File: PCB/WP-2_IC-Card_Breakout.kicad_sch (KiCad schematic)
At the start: 2 parts, among them J1 Conn_01x38_Female, J2 Conn_02x19_Odd_Even

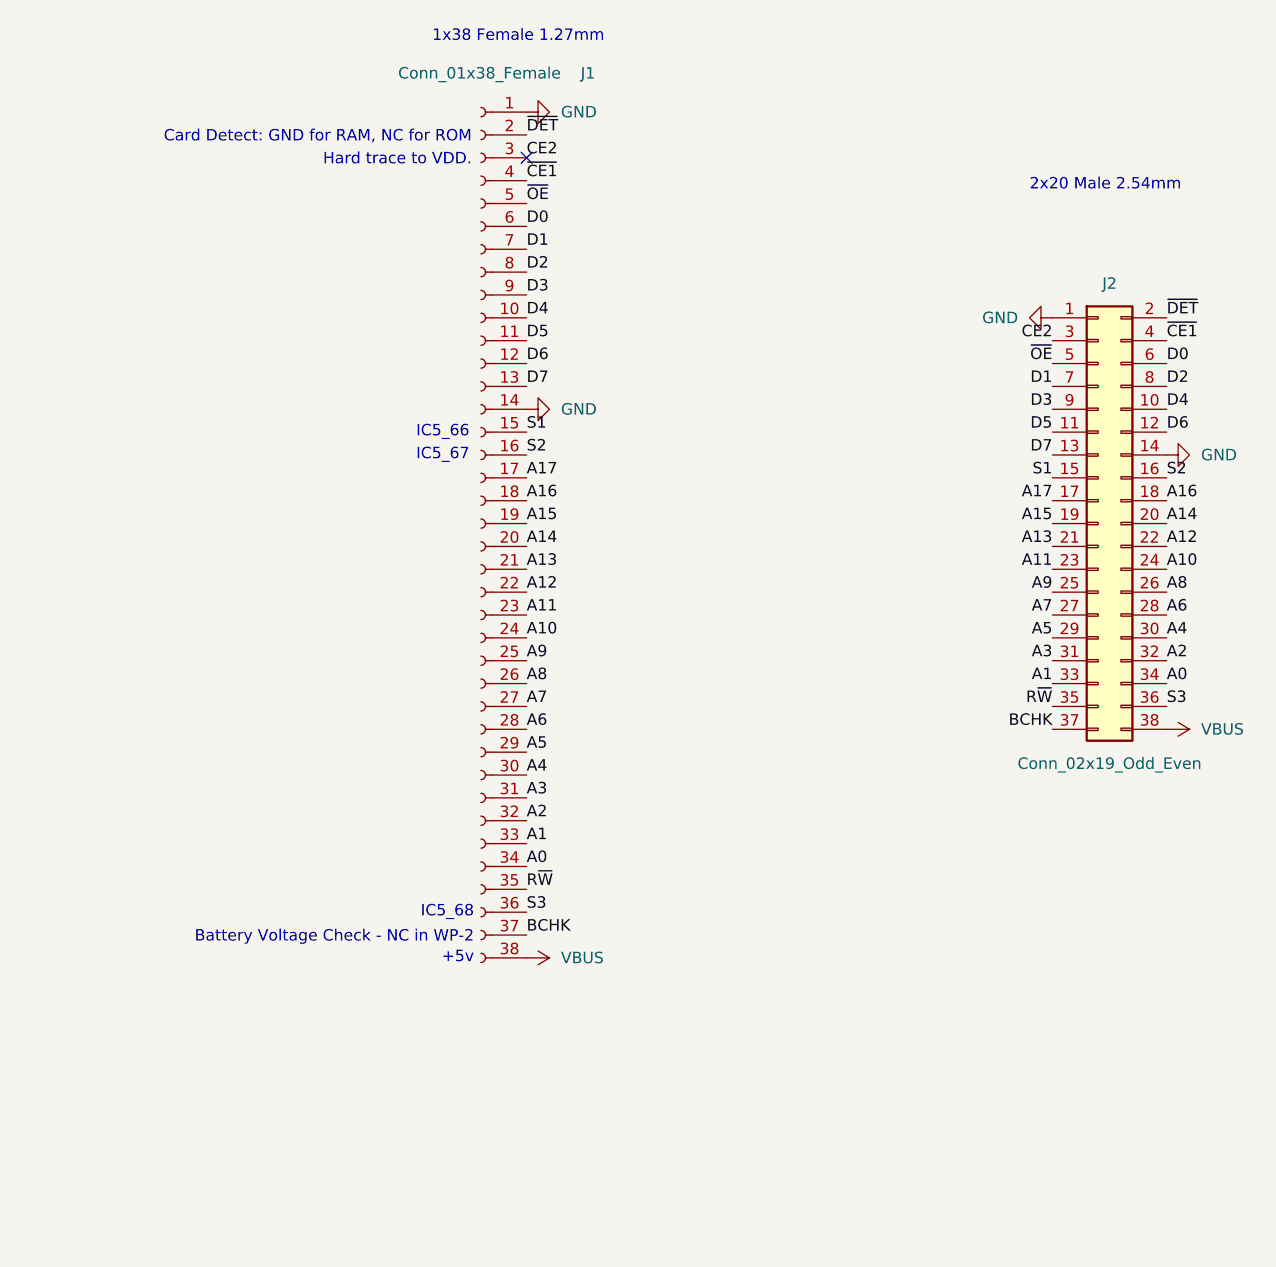
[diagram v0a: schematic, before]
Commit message: MRAM level shifters, delete FRAM, local datasheets in local symbols
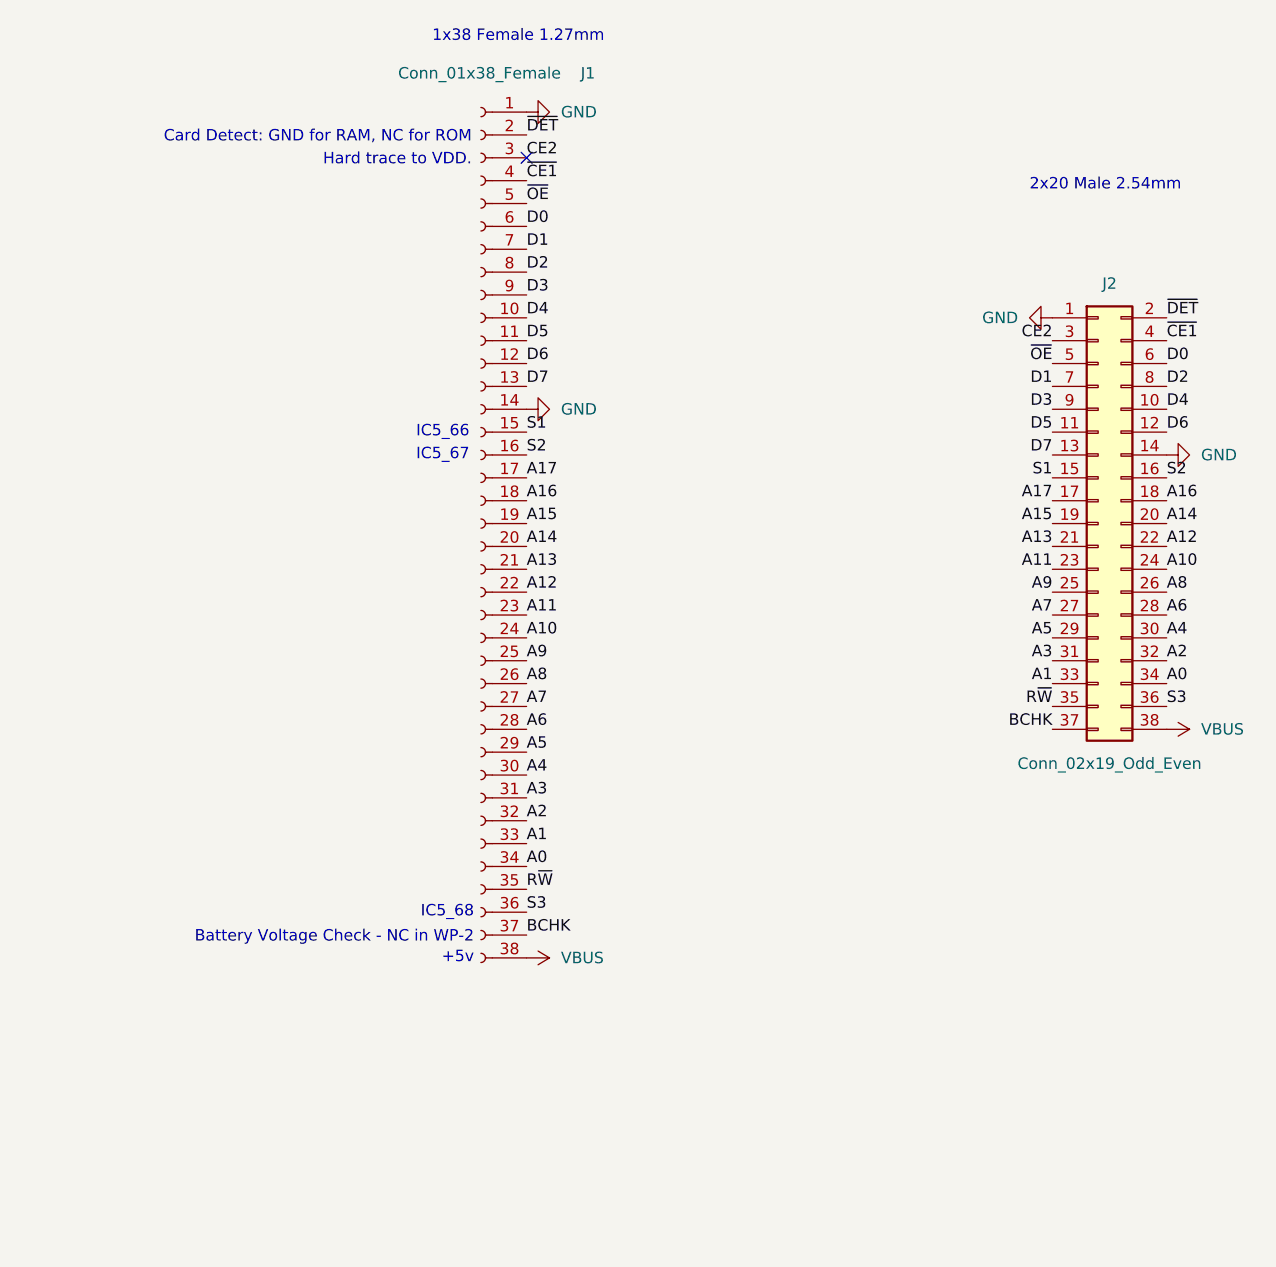
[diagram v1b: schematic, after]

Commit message: local symbol & footprint library organization, add shielded mram version
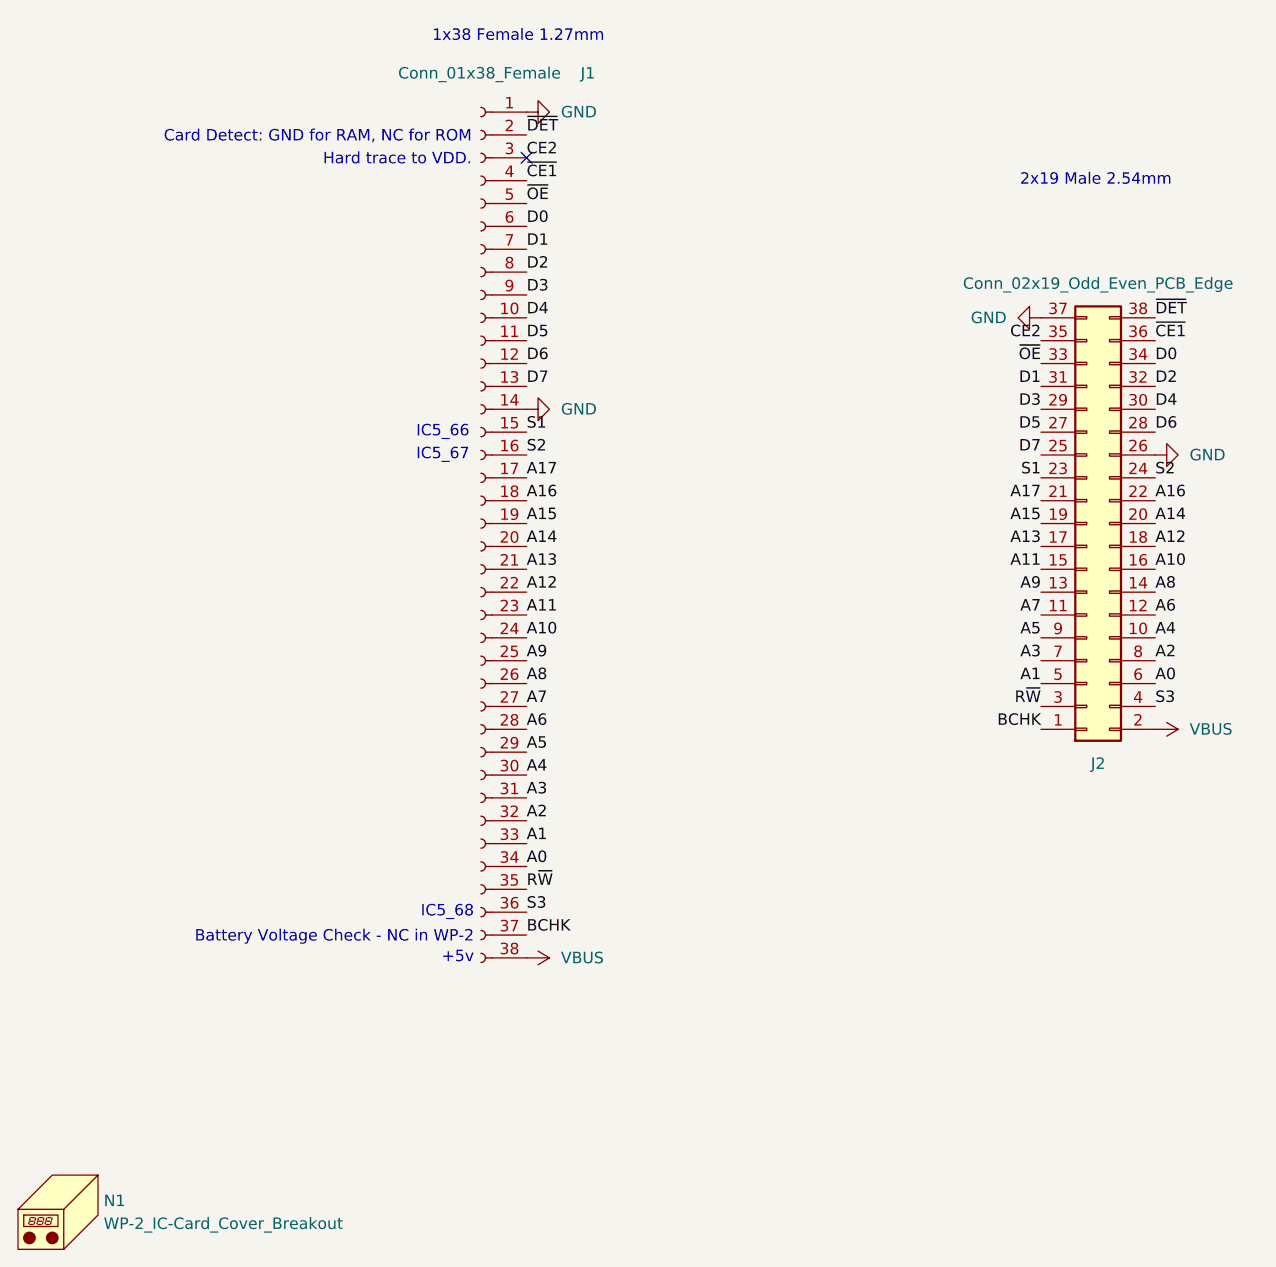
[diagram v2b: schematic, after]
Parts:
- added N1: WP-2_IC-Card_Cover_Breakout, 000_LOCAL:WP-2_IC_Card_Cover_Breakout, symbol 000_LOCAL:Housing
- J1: footprint 0_LOCAL:SMS-138-01-x-x_edge -> 000_LOCAL:SMS-138-01-x-x_pcb_edge; symbol 0_LOCAL:Conn_01x38_Female -> 000_LOCAL:Conn_01x38_Female
- J2: value Conn_02x19_Odd_Even -> Conn_02x19_Odd_Even_PCB_Edge; footprint 0_LOCAL:PinHeader_2x19_P2.54mm -> 000_LOCAL:Pin-Header_2x19_P2.54mm_PCB_Edge; symbol 0_LOCAL:Conn_02x19_Odd_Even -> 000_LOCAL:Conn_02x19_Odd_Even
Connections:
- net A0: now also J2.6 (Pin_6); no longer J2.34 (Pin_34)
- net A1: now also J2.5 (Pin_5); no longer J2.33 (Pin_33)
- net A10: now also J2.16 (Pin_16); no longer J2.24 (Pin_24)
- net A11: now also J2.15 (Pin_15); no longer J2.23 (Pin_23)
- net A12: now also J2.18 (Pin_18); no longer J2.22 (Pin_22)
- net A13: now also J2.17 (Pin_17); no longer J2.21 (Pin_21)
- net A16: now also J2.22 (Pin_22); no longer J2.18 (Pin_18)
- net A17: now also J2.21 (Pin_21); no longer J2.17 (Pin_17)
- net A2: now also J2.8 (Pin_8); no longer J2.32 (Pin_32)
- net A3: now also J2.7 (Pin_7); no longer J2.31 (Pin_31)
- net A4: now also J2.10 (Pin_10); no longer J2.30 (Pin_30)
- net A5: now also J2.9 (Pin_9); no longer J2.29 (Pin_29)
- net A6: now also J2.12 (Pin_12); no longer J2.28 (Pin_28)
- net A7: now also J2.11 (Pin_11); no longer J2.27 (Pin_27)
- net A8: now also J2.14 (Pin_14); no longer J2.26 (Pin_26)
- net A9: now also J2.13 (Pin_13); no longer J2.25 (Pin_25)
- net BCHK: now also J2.1 (Pin_1); no longer J2.37 (Pin_37)
- net CE2: now also J2.35 (Pin_35); no longer J2.3 (Pin_3)
- net D0: now also J2.34 (Pin_34); no longer J2.6 (Pin_6)
- net D1: now also J2.31 (Pin_31); no longer J2.7 (Pin_7)
- net D2: now also J2.32 (Pin_32); no longer J2.8 (Pin_8)
- net D3: now also J2.29 (Pin_29); no longer J2.9 (Pin_9)
- net D4: now also J2.30 (Pin_30); no longer J2.10 (Pin_10)
- net D5: now also J2.27 (Pin_27); no longer J2.11 (Pin_11)
- net D6: now also J2.28 (Pin_28); no longer J2.12 (Pin_12)
- net D7: now also J2.25 (Pin_25); no longer J2.13 (Pin_13)
- net GND: now also J2.26 (Pin_26), J2.37 (Pin_37); no longer J2.1 (Pin_1), J2.14 (Pin_14)
- net R~{W}: now also J2.3 (Pin_3); no longer J2.35 (Pin_35)
- net S1: now also J2.23 (Pin_23); no longer J2.15 (Pin_15)
- net S2: now also J2.24 (Pin_24); no longer J2.16 (Pin_16)
- net S3: now also J2.4 (Pin_4); no longer J2.36 (Pin_36)
- net VBUS: now also J2.2 (Pin_2); no longer J2.38 (Pin_38)
- net ~{CE1}: now also J2.36 (Pin_36); no longer J2.4 (Pin_4)
- net ~{DET}: now also J2.38 (Pin_38); no longer J2.2 (Pin_2)
- net ~{OE}: now also J2.33 (Pin_33); no longer J2.5 (Pin_5)
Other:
- note added: "2x19 Male 2.54mm"
- note removed: "2x20 Male 2.54mm"
- moved on the sheet: J2

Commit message: cleanup names, cover inside corner reliefs
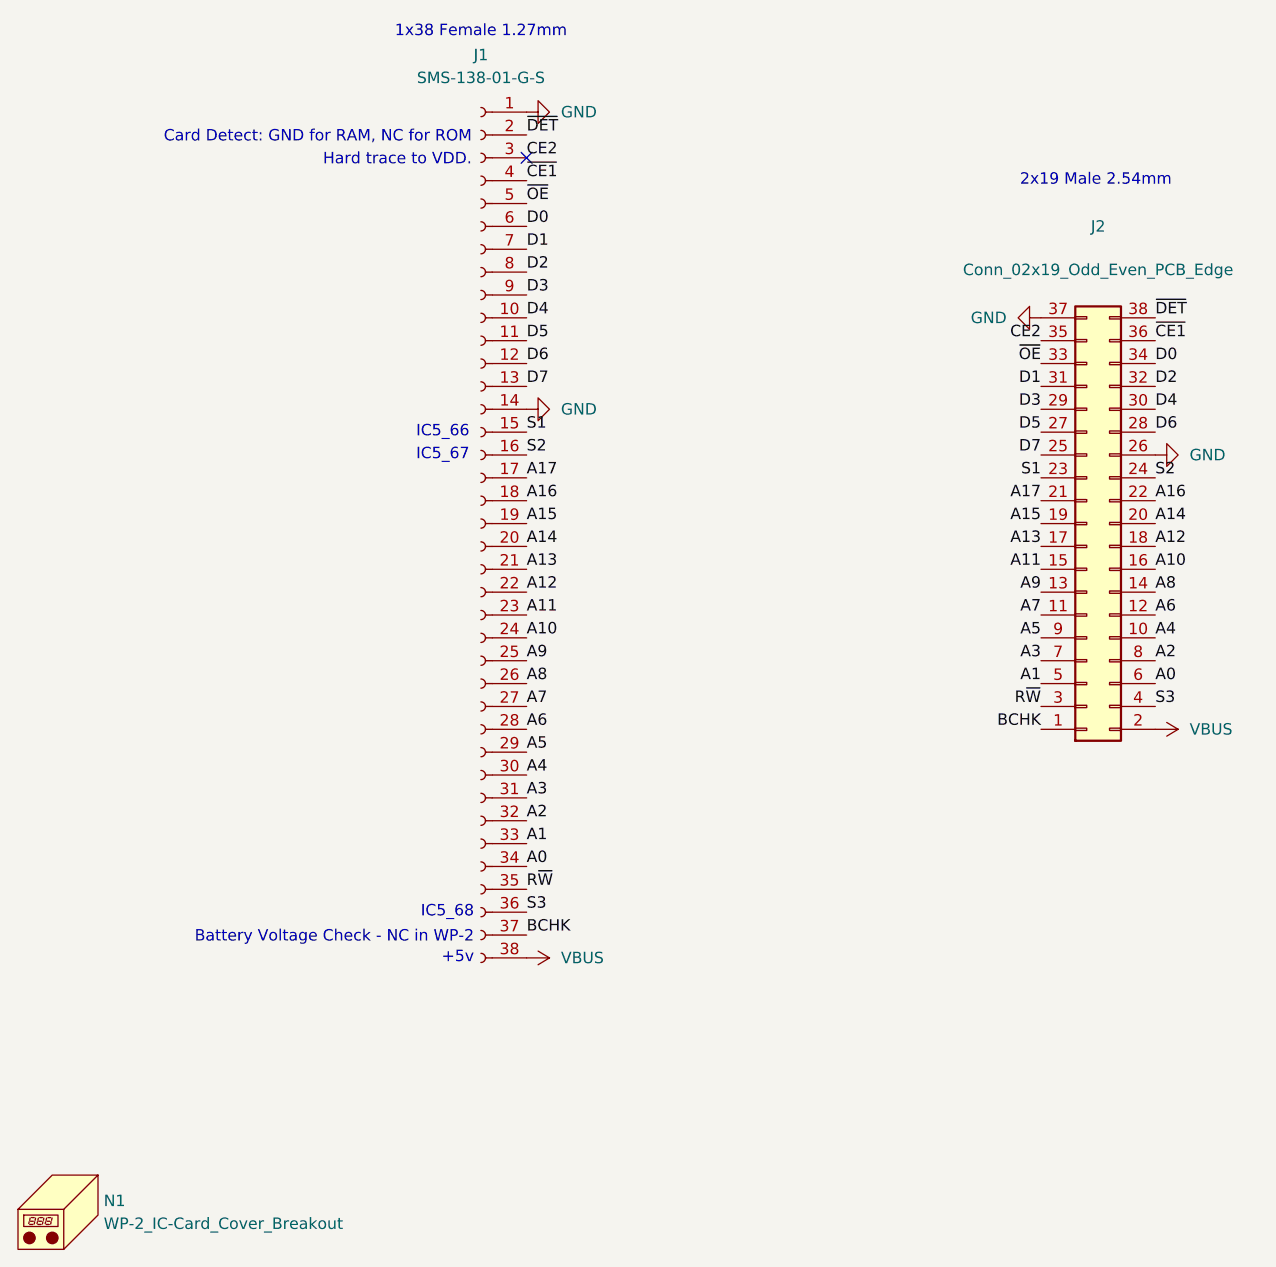
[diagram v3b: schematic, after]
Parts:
- J1: value Conn_01x38_Female -> SMS-138-01-G-S; MPN (none) -> SMS-138-01-G-S
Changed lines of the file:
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@@
 	(text "1x38 Female 1.27mm"
 		(exclude_from_sim no)
-		(at 122.936 48.26 0)
-		(effects
-			(font
-				(size 1.27 1.27)
-			)
-			(justify right bottom)
+		(at 109.22 46.99 0)
+		(effects
+			(font
+				(size 1.27 1.27)
+			)
 		)
 	)
@@
 		(dnp no)
 		(property "Reference" "J1"
-			(at 121.92 51.562 0)
-			(effects
-				(font
-					(size 1.27 1.27)
-				)
-				(justify left)
-			)
-		)
-		(property "Value" "Conn_01x38_Female"
-			(at 118.11 51.562 0)
-			(effects
-				(font
-					(size 1.27 1.27)
-				)
-				(justify left)
+			(at 109.22 49.53 0)
+			(effects
+				(font
+					(size 1.27 1.27)
+				)
+			)
+		)
+		(property "Value" "SMS-138-01-G-S"
+			(at 109.22 52.07 0)
+			(effects
+				(font
+					(size 1.27 1.27)
+				)
 			)
 		)
@@
 		)
 		(property "Description" ""
+			(at 109.22 101.6 0)
+			(effects
+				(font
+					(size 1.27 1.27)
+				)
+				(hide yes)
+			)
+		)
+		(property "MPN" "SMS-138-01-G-S"
 			(at 109.22 101.6 0)
 			(effects
@@
 		(dnp no)
 		(property "Reference" "J2"
-			(at 177.8 128.27 0)
+			(at 177.8 68.58 0)
 			(effects
 				(font
@@
 		)
 		(property "Value" "Conn_02x19_Odd_Even_PCB_Edge"
-			(at 177.8 74.93 0)
-			(effects
-				(font
+			(at 177.8 73.406 0)
+			(effects
+				(font
